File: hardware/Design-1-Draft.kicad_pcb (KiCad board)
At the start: 2 copper layers, 26 parts, among them J1 Barrel_Jack_Switch, Q1 IRLZ44N, Q2 IRLZ44N, U3 ADS1115IDGS, U5 Tang_Nano_9K

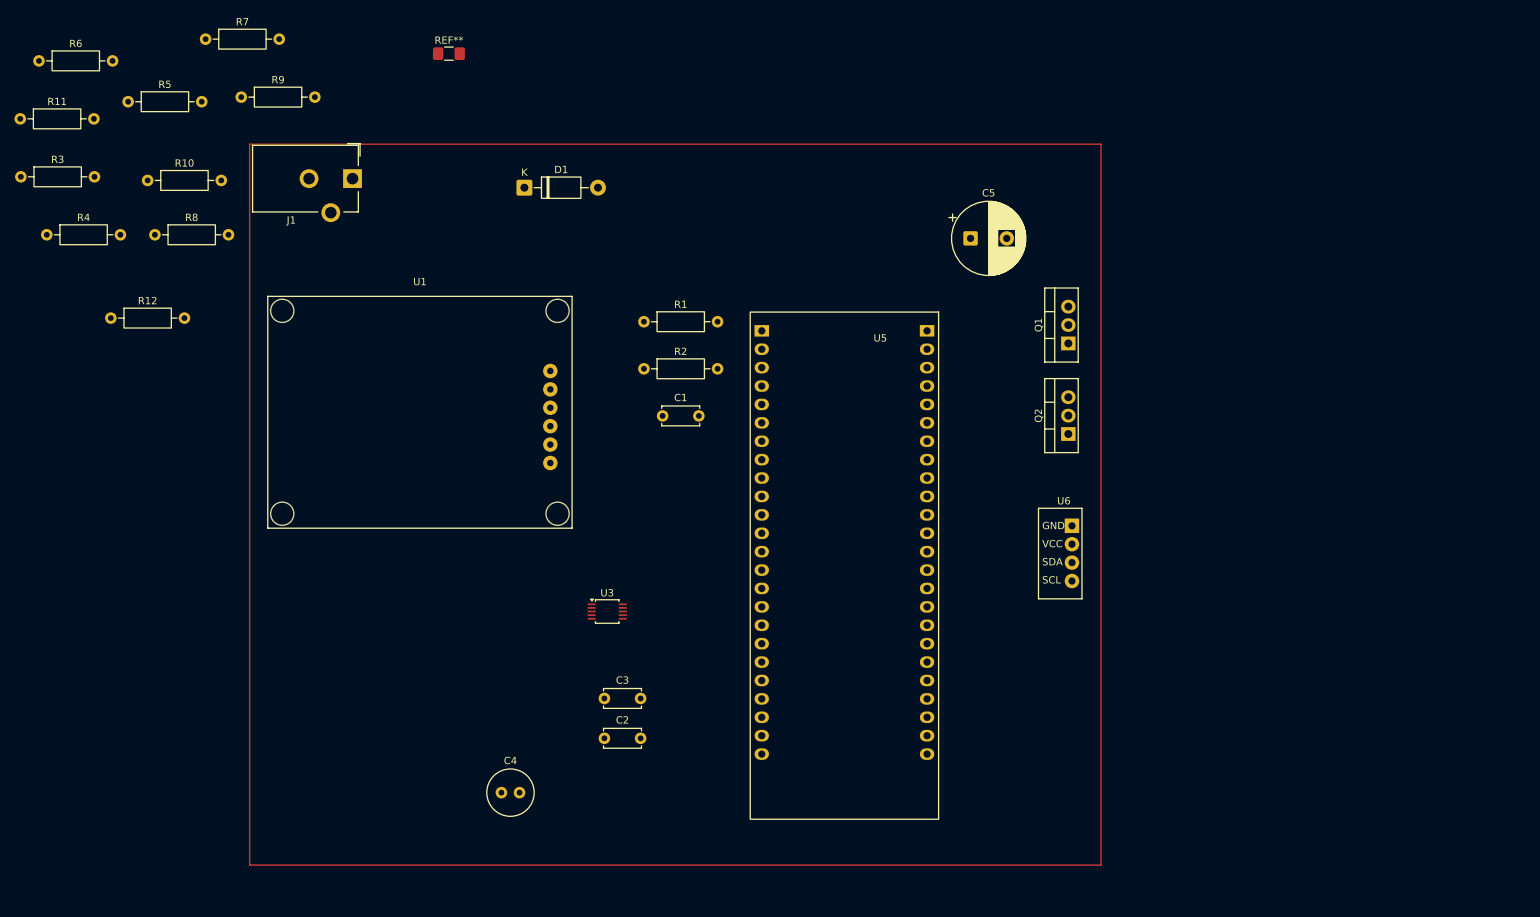
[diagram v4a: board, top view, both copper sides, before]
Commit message: updated footprints
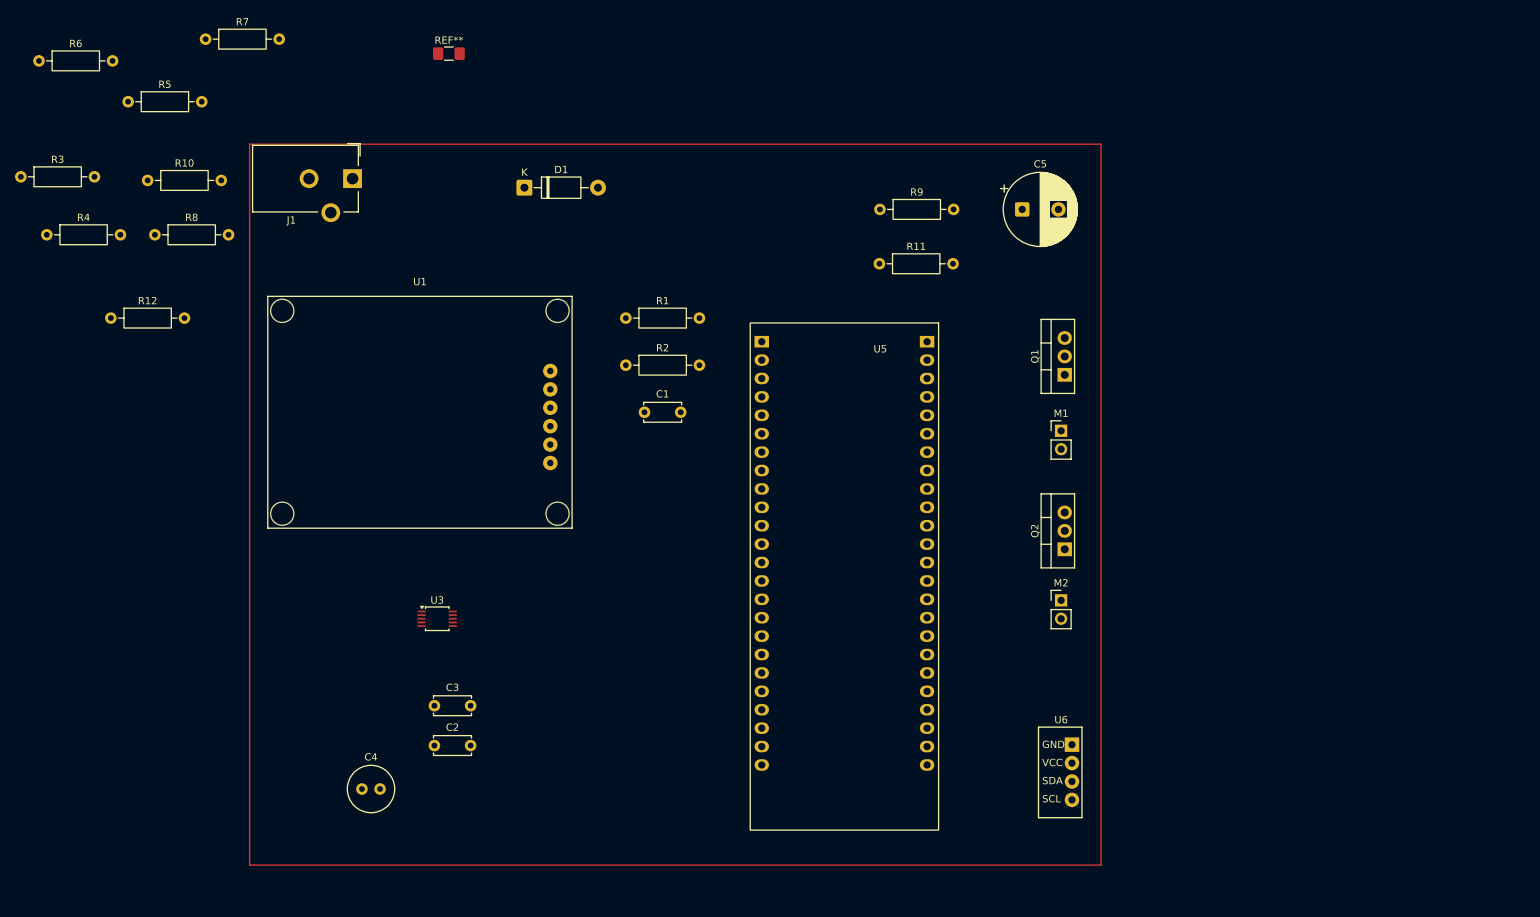
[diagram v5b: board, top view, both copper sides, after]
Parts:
- added M1: WATERPUMP-1, Connector_PinHeader_2.54mm:PinHeader_1x02_P2.54mm_Vertical, F.Cu at (178.5, 73.6)
- added M2: WATERPUMP-2, Connector_PinHeader_2.54mm:PinHeader_1x02_P2.54mm_Vertical, F.Cu at (178.5, 97.0)
- moved R11 120.3 mm to (153.4, 50.5)
- moved R9 89.5 mm to (153.5, 43.0)
- moved U6 30.2 mm to (178.5, 120.7)
- moved C2 23.5 mm to (92.0, 117.0)
- moved C3 23.5 mm to (92.0, 111.5)
- moved U3 23.5 mm to (92.4, 99.5)
- moved C4 19.3 mm to (82.0, 123.0)
- moved Q2 15.9 mm to (179.0, 89.9)
- moved C5 8.18 mm to (173.1, 43.0)
- moved Q1 4.36 mm to (179.0, 65.8)
- moved C1 2.55 mm to (121.0, 71.0)
- moved R1 2.55 mm to (118.4, 58.0)
- moved R2 2.55 mm to (118.4, 64.5)
- moved U5 1.50 mm to (148.6, 90.5)

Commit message: some updates footprint and pcb
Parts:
- added BZ1: Buzzer, Connector_PinHeader_2.54mm:PinHeader_1x02_P2.54mm_Vertical, F.Cu at (36.4, 79.8)
- added F1: Fuse, Fuse:Fuseholder_Clip-5x20mm_Keystone_3512P_Inline_P23.62x7.27mm_D1.02x2.41x1.02x1.57mm_Horizontal, F.Cu at (88.2, 39.0)
- added SW1: Button, Connector_PinHeader_2.54mm:PinHeader_1x02_P2.54mm_Vertical, F.Cu at (41.0, 79.8)
- moved D1 15.5 mm to (119.9, 39.0)

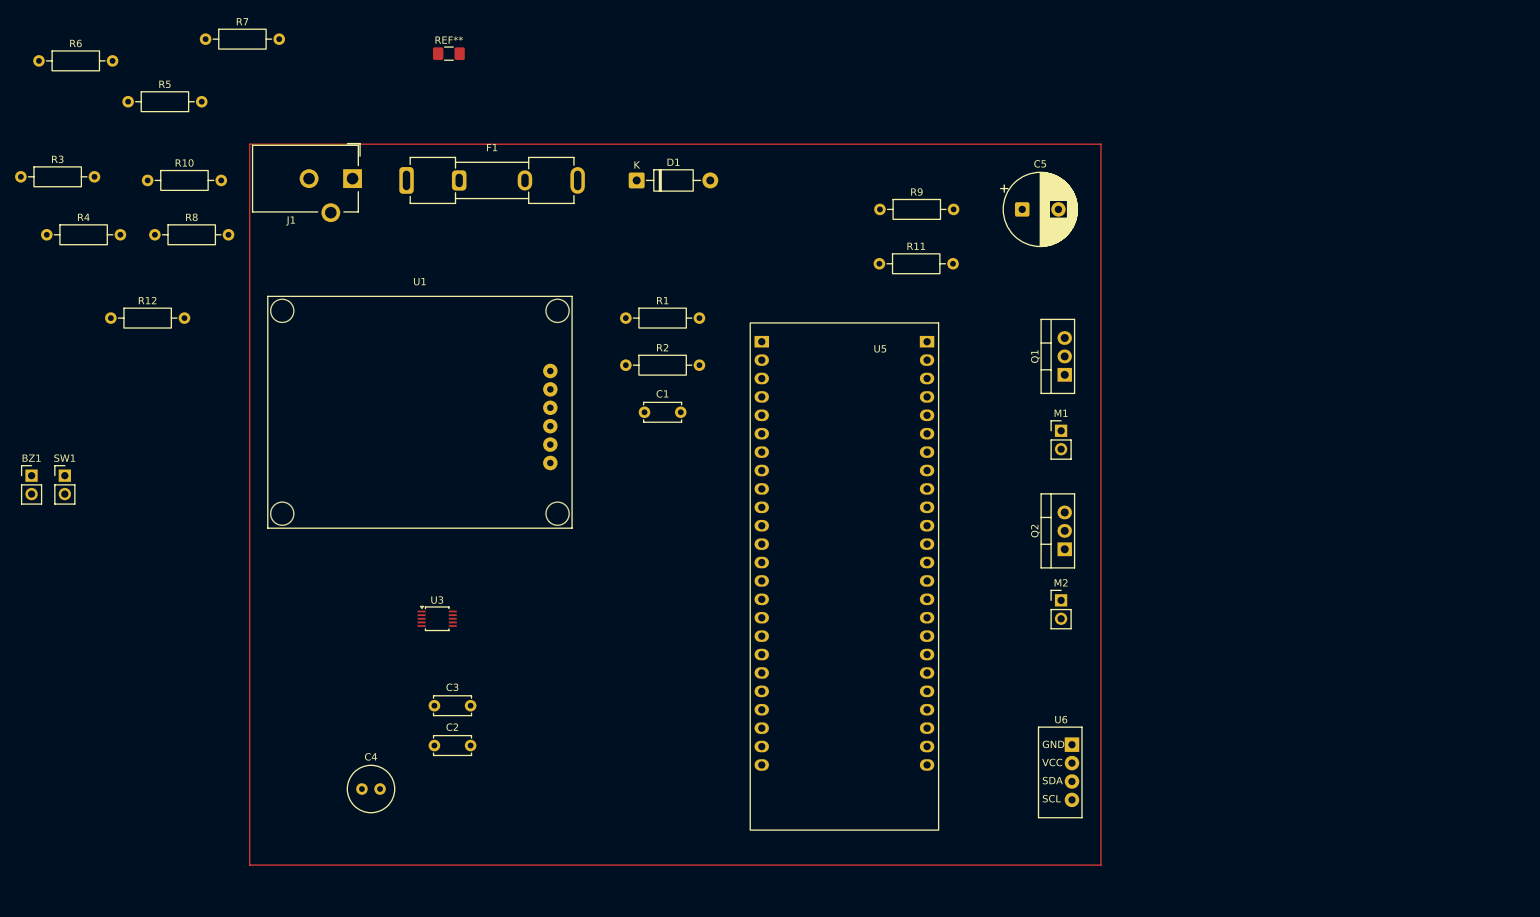
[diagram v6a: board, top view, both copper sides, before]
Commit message: Updated Footprint Library for custom footprints. Fixed PCB footprints, traces nalang kulang
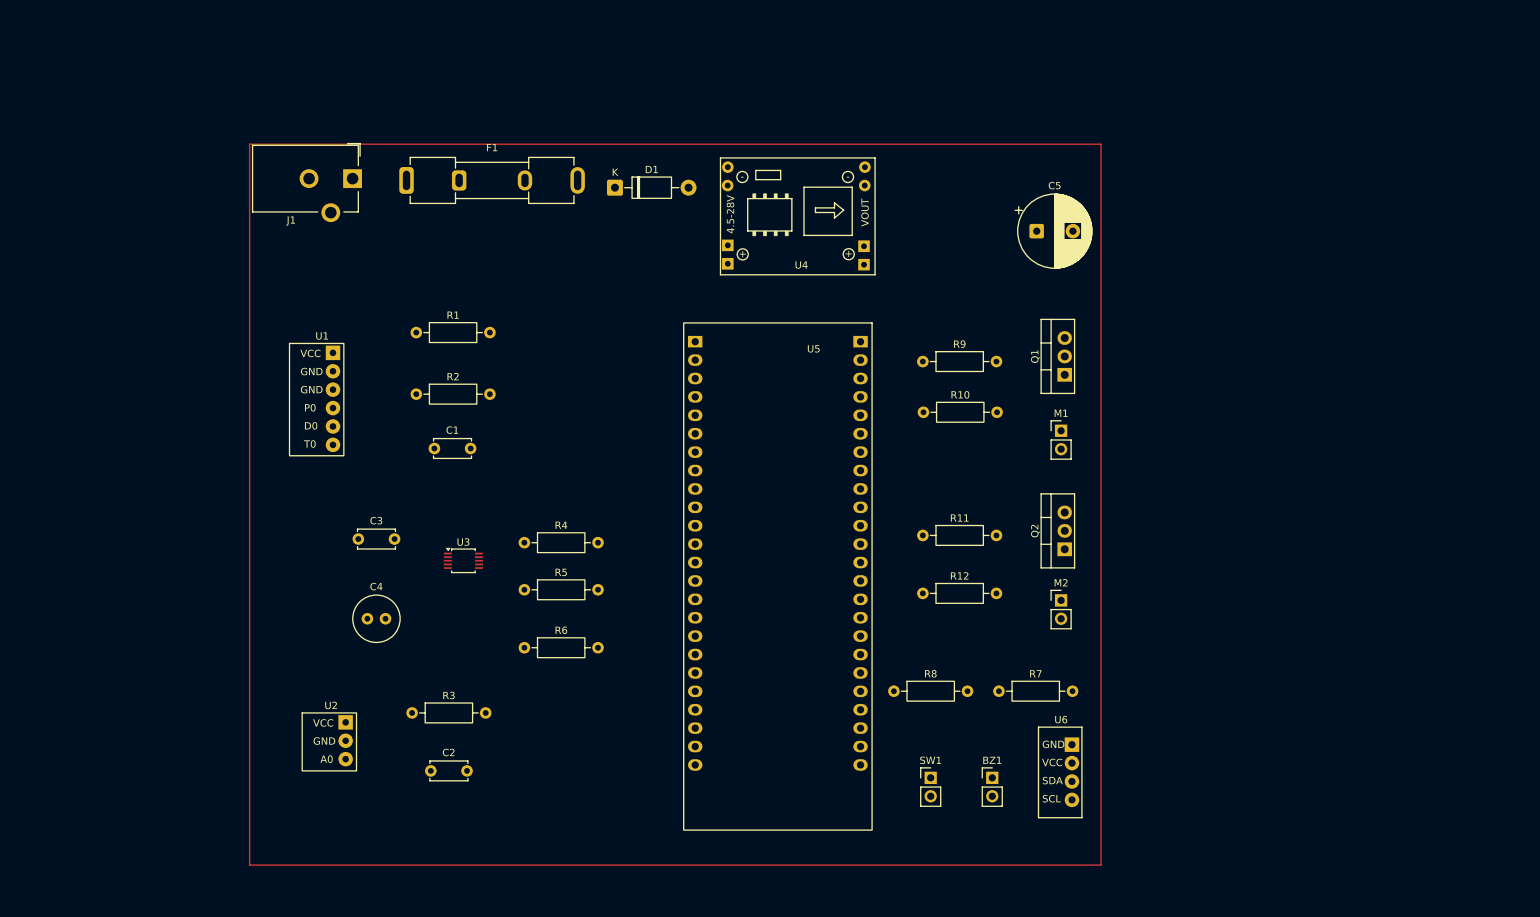
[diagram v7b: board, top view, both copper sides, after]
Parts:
- removed REF**: Fuse_1206_3216Metric_Pad1.42x1.75mm_HandSolder, Fuse:Fuse_1206_3216Metric_Pad1.42x1.75mm_HandSolder
- added U2: ~, 1_CustomFootprints:TDS-ANALOG-SENSOR, F.Cu at (77.5, 116.5)
- added U4: ~, 1_CustomFootprints:SRT_MPT1584EN_Module, F.Cu at (142.7, 43.4)
- moved R7 141.7 mm to (169.9, 109.5)
- moved BZ1 139.0 mm to (169.0, 121.5)
- moved SW1 126.6 mm to (160.5, 121.5)
- moved R8 119.9 mm to (155.4, 109.5)
- moved R12 118.3 mm to (159.4, 96.0)
- moved R10 111.8 mm to (159.5, 71.0)
- moved R6 105.1 mm to (104.4, 103.5)
- moved R3 91.6 mm to (88.9, 112.5)
- moved R5 86.8 mm to (104.4, 95.5)
- moved R4 78.4 mm to (104.4, 89.0)
- moved R11 38.0 mm to (159.4, 88.0)
- moved C1 29.4 mm to (92.0, 76.0)
- moved R2 29.2 mm to (89.5, 68.5)
- moved R1 29.0 mm to (89.5, 60.0)
- moved C3 25.3 mm to (81.5, 88.5)
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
